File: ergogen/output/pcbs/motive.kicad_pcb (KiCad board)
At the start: 2 copper layers, 220.4 x 89.6 mm, 40 parts

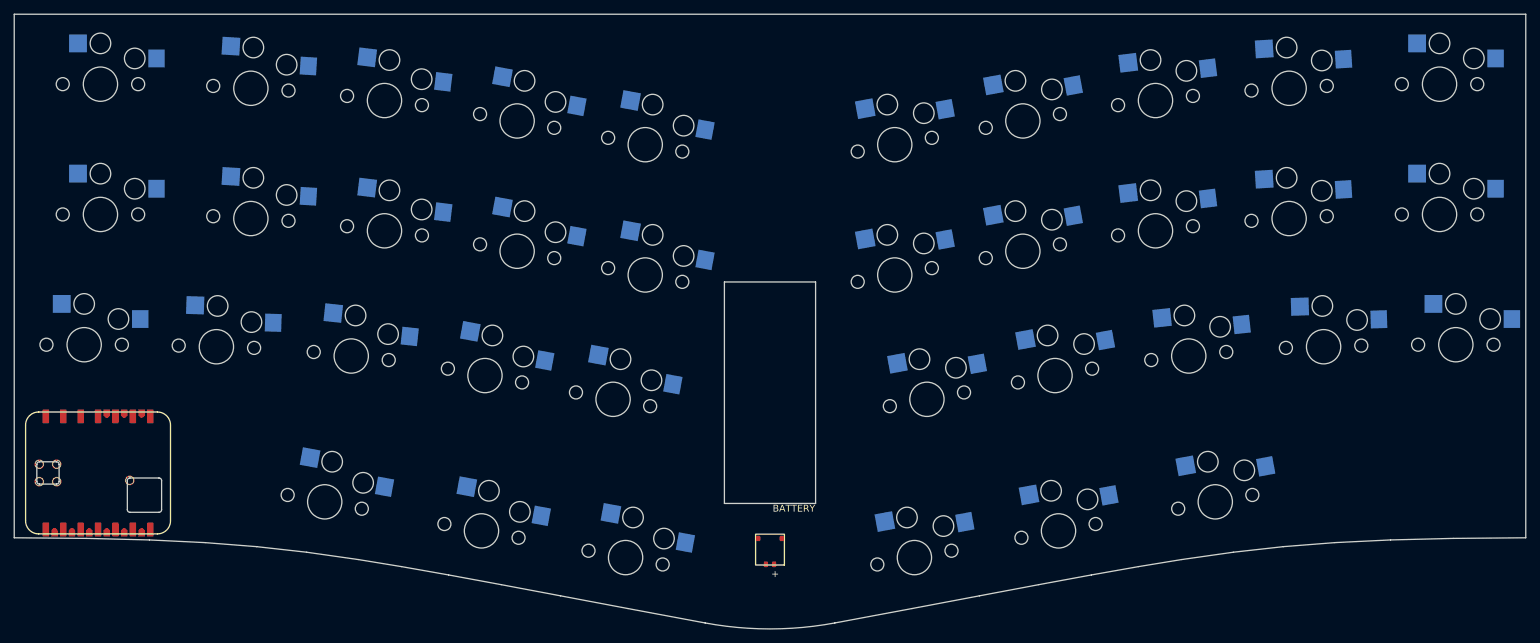
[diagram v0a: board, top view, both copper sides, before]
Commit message: updated footprint models
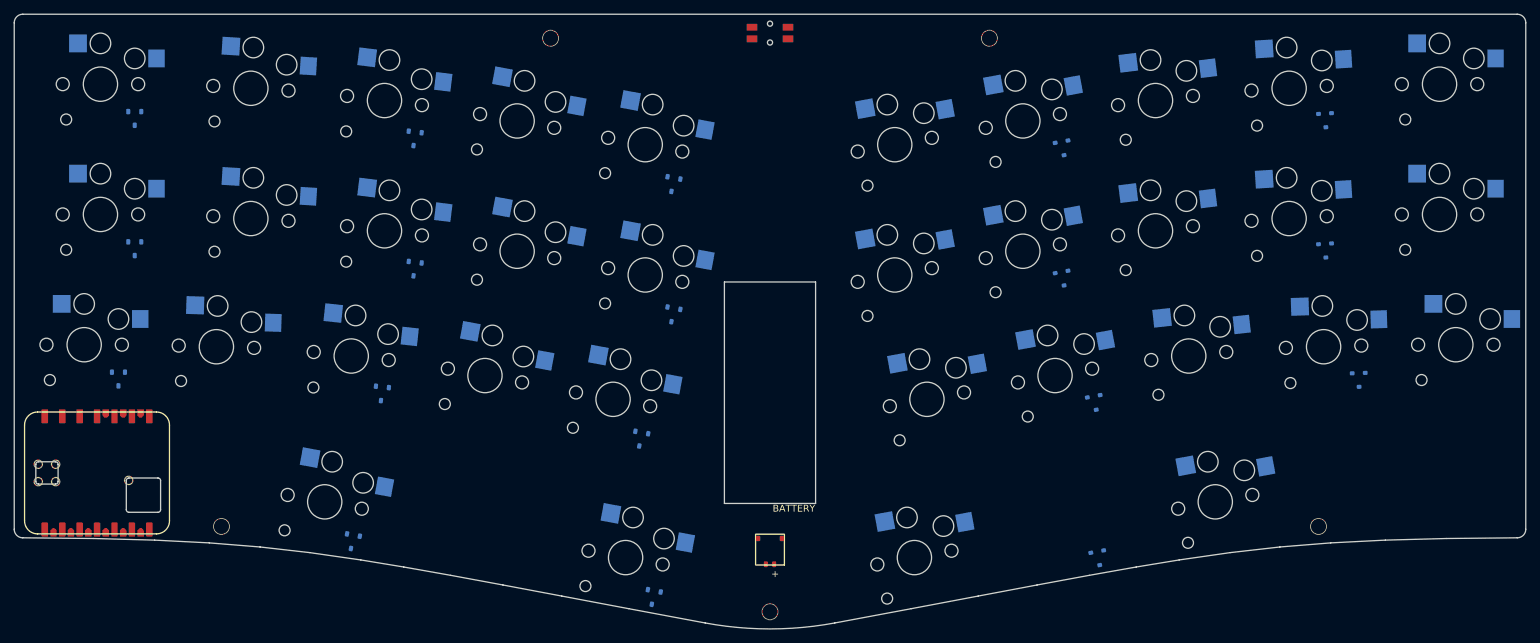
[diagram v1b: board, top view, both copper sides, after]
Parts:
- removed CONN1: , conn_molex_pico_front
- removed S1, S10, S11, S12, S13, S14, S15, S16, S17, S18, S19, S2, S20, S21, S22, S23, S24, S25, S26, S27, S28, S29, S3, S30, S31, S32, S33, S34, S35, S36, S4, S5, S6, S7, S8, S9: , ceoloide:switch_choc_v1_v2
- removed XX3: , xiao_plus_smd_prod
- added D1: , SOT-23, B.Cu at (5.00, 5.00)
- added D10: , SOT-23, B.Cu at (36.7, 66.7)
- added D11: , SOT-23, B.Cu at (80.6, 74.9)
- added D12: , SOT-23, B.Cu at (178.7, 5.28)
- added D13: , SOT-23, B.Cu at (140.4, 9.37)
- added D14: , SOT-23, B.Cu at (178.7, 24.3)
- added D15: , SOT-23, B.Cu at (140.4, 28.4)
- added D16: , SOT-23, B.Cu at (183.5, 43.1)
- added D17: , SOT-23, B.Cu at (145.0, 46.5)
- added D18: , SOT-23, B.Cu at (145.6, 69.2)
- added D2: , SOT-23, B.Cu at (45.8, 7.96)
- added D3: , SOT-23, B.Cu at (83.5, 14.7)
- added D4: , SOT-23, B.Cu at (5.00, 24.0)
- added D5: , SOT-23, B.Cu at (45.8, 27.0)
- added D6: , SOT-23, B.Cu at (83.5, 33.7)
- added D7: , SOT-23, B.Cu at (2.62, 43.0)
- added D8: , SOT-23, B.Cu at (41.0, 45.2)
- added D9: , SOT-23, B.Cu at (78.8, 51.8)
- added EC1: , pcb_shape, F.Cu at (0.00, 0.00)
- added H1: , mounting_hole, F.Cu at (65.6, -6.70)
- added H2: , mounting_hole, F.Cu at (129.6, -6.70)
- added H3: , mounting_hole, F.Cu at (17.6, 64.5)
- added H4: , mounting_hole, F.Cu at (97.6, 76.9)
- added H5: , mounting_hole, F.Cu at (177.6, 64.5)
- added MCU1: , xiao_plus_smd_prod, F.Cu at (-0.50, 56.7)
- added SW1: , choc, F.Cu at (32.7, 60.9)
- added SW10: , sw_choc_1u, F.Cu at (115.8, 8.83)
- added SW11: , sw_choc_1u, F.Cu at (21.9, 19.6)
- added SW12: , sw_choc_1u, F.Cu at (41.4, 21.4)
- added SW13: , sw_choc_1u, F.Cu at (60.8, 24.4)
- added SW14: , sw_choc_1u, F.Cu at (79.5, 27.8)
- added SW15: , sw_choc_1u, F.Cu at (173.4, 19.6)
- added SW16: , sw_choc_1u, F.Cu at (153.9, 21.4)
- added SW17: , sw_choc_1u, F.Cu at (134.5, 24.4)
- added SW18: , sw_choc_1u, F.Cu at (115.8, 27.8)
- added SW19: , sw_choc_1u, F.Cu at (-2.38, 38.0)
- added SW2: , choc, F.Cu at (162.6, 60.9)
- added SW20: , sw_choc_1u, F.Cu at (16.9, 38.3)
- added SW21: , sw_choc_1u, F.Cu at (36.6, 39.6)
- added SW22: , sw_choc_1u, F.Cu at (56.1, 42.5)
- added SW23: , sw_choc_1u, F.Cu at (74.8, 46.0)
- added SW24: , sw_choc_1u, F.Cu at (197.7, 38.0)
- added SW25: , sw_choc_1u, F.Cu at (178.4, 38.3)
- added SW26: , sw_choc_1u, F.Cu at (158.7, 39.6)
- added SW27: , sw_choc_1u, F.Cu at (139.2, 42.5)
- added SW28: , sw_choc_1u, F.Cu at (120.5, 46.0)
- added SW29: , sw_choc_1.25u, F.Cu at (0.00, 0.00)
- added SW3: , sw_choc_1u, F.Cu at (21.9, 0.60)
- added SW30: , sw_choc_1.25u, F.Cu at (195.3, 0.00)
- added SW31: , sw_choc_1.25u, F.Cu at (0.00, 19.0)
- added SW32: , sw_choc_1.25u, F.Cu at (195.3, 19.0)
- added SW33: , sw_choc_1.25u, F.Cu at (76.6, 69.0)
- added SW34: , sw_choc_1.25u, F.Cu at (118.7, 69.0)
- added SW4: , sw_choc_1u, F.Cu at (41.4, 2.39)
- added SW5: , sw_choc_1u, F.Cu at (60.8, 5.37)
- added SW6: , sw_choc_1u, F.Cu at (79.5, 8.83)
- added SW7: , sw_choc_1u, F.Cu at (173.4, 0.60)
- added SW8: , sw_choc_1u, F.Cu at (153.9, 2.39)
- added SW9: , sw_choc_1u, F.Cu at (134.5, 5.37)
- XX1: footprint pcb_shape -> sw_reset_side
- XX2: footprint keywall -> conn_molex_pico_front
- moved XX2 119.1 mm to (97.6, 68.2), turned to 180 degrees
- moved XX1 97.9 mm to (97.6, -7.45)
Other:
- outline, holes or cut-outs redrawn
